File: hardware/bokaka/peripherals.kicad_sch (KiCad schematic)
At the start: 7 parts, among them SW1 SW_MEC_5G, SW2 SW_MEC_5G, SW3 SW_MEC_5G, U3 IS31FL3236A-TQ

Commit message: Finalize design before pcb
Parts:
- removed SW1, SW2, SW3: SW_MEC_5G, symbol Switch:SW_MEC_5G
- removed U3: IS31FL3236A-TQ, Package_QFP:TQFP-48-1EP_7x7mm_P0.5mm_EP4.11x4.11mm, symbol Driver_LED:IS31FL3236A-TQ
- added C12, C14, C22: 0.1u, Capacitor_SMD:C_0402_1005Metric, symbol Device:C
- added C13: 1u, Capacitor_SMD:C_0402_1005Metric, symbol Device:C
- added D10, D11, D12, D13, D14, D15, D16, D17, D18, D19, D2, D20, D21, D22, D23, D24, D25, D26, D27, D28, D29, D3, D30, D31, D32, D33, D34, D35, D36, D37, D38, D4, D5, D6, D7, D8, D9: LED, symbol Device:LED
- added R6: 1k5, Resistor_SMD:R_0402_1005Metric, symbol Device:R
- added R7: 10K, Resistor_SMD:R_0402_1005Metric, symbol Device:R
- added SW1, SW2, SW3: ~, EasyEDA_Lib:SW-SMD_4P-L5.1-W5.1-P3.70-LS6.5-TL_H1.5, symbol EasyEDA_Lib:TS-1187A-B-A-B
- added U1: IS31FL3236A-QFLS2-TR, Footprints:QFN40P500X500X80-45N, symbol Symbols:IS31FL3236A-QFLS2-TR
- BZ1: footprint (none) -> Footprints:CUI_CPT-9019S-SMT
- R4: footprint (none) -> Resistor_SMD:R_0402_1005Metric
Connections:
- net GND: now also C12.2, C13.2, C14.2, C22.2, R6.2, R7.2, SW1.4 (D), SW2.4 (D), SW3.4 (D), U1.17 (GND), U1.37 (AD), U1.39 (GND), U1.45 (EXP_PAD)
- net LED_I2C_SCL: now also U1.42 (SCL)
- net LED_I2C_SDA: now also U1.41 (SDA)
- net USR_BTN0: now also C14.1, SW2.1 (A)
- net USR_BTN1: now also C22.1, SW3.1 (A)
- net ~{BOOT_SEL}: now also SW1.1 (A)
- new net: D5.1 (K), U1.1 (OUT3)
- new net: D27.1 (K), U1.28 (OUT29)
- new net: D17.1 (K), U1.13 (OUT15)
- new net: R7.1, U1.40 (R_EXT)
- new net: D18.1 (K), U1.14 (OUT16)
- new net: D25.1 (K), U1.26 (OUT27)
- new net: D14.1 (K), U1.10 (OUT12)
- new net: D15.1 (K), U1.11 (OUT13)
- new net: D13.1 (K), U1.9 (OUT11)
- new net: D2.1 (K), R6.1
- new net: D20.1 (K), U1.16 (OUT18)
- new net: D11.1 (K), U1.7 (OUT9)
- new net: D26.1 (K), U1.27 (OUT28)
- new net: D6.1 (K), U1.2 (OUT4)
- new net: D16.1 (K), U1.12 (OUT14)
- new net: D19.1 (K), U1.15 (OUT17)
- new net: D38.1 (K), U1.35 (OUT36)
- new net: D7.1 (K), U1.3 (OUT5)
- new net: D33.1 (K), U1.22 (OUT23)
- new net: D28.1 (K), U1.29 (OUT30)
- new net: D22.1 (K), U1.19 (OUT20)
- new net: D21.1 (K), U1.18 (OUT19)
- new net: D32.1 (K), U1.31 (OUT32)
- new net: D23.1 (K), U1.24 (OUT25)
- new net: D9.1 (K), U1.5 (OUT7)
- new net: D12.1 (K), U1.8 (OUT10)
- new net: D29.1 (K), U1.20 (OUT21)
- new net: D31.1 (K), U1.21 (OUT22)
- new net: D36.1 (K), U1.23 (OUT24)
- new net: D24.1 (K), U1.25 (OUT26)
- new net: D30.1 (K), U1.30 (OUT31)
- new net: D34.1 (K), U1.32 (OUT33)
- new net: D37.1 (K), U1.33 (OUT34)
- new net: D35.1 (K), U1.34 (OUT35)
- new net: D8.1 (K), U1.4 (OUT6)
- new net: D4.1 (K), U1.44 (OUT2)
- new net: D10.1 (K), U1.6 (OUT8)
- new net +3V3: C12.1, C13.1, D10.2 (A), D11.2 (A), D12.2 (A), D13.2 (A), D14.2 (A), D15.2 (A), D16.2 (A), D17.2 (A), D18.2 (A), D19.2 (A), D20.2 (A), D21.2 (A), D22.2 (A), D23.2 (A), D24.2 (A), D25.2 (A), D26.2 (A), D27.2 (A), D28.2 (A), D29.2 (A), D3.2 (A), D30.2 (A), D31.2 (A), D32.2 (A), D33.2 (A), D34.2 (A), D35.2 (A), D36.2 (A), D37.2 (A), D38.2 (A), D4.2 (A), D5.2 (A), D6.2 (A), D7.2 (A), D8.2 (A), D9.2 (A), U1.38 (VCC)
- new net LED_DEBUG: D2.2 (A)
- new net LED_EN: U1.36 (SDB)
- new net PROGRESS_LED_0: D3.1 (K), U1.43 (OUT1)
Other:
- moved on the sheet: BZ1, D1, R4

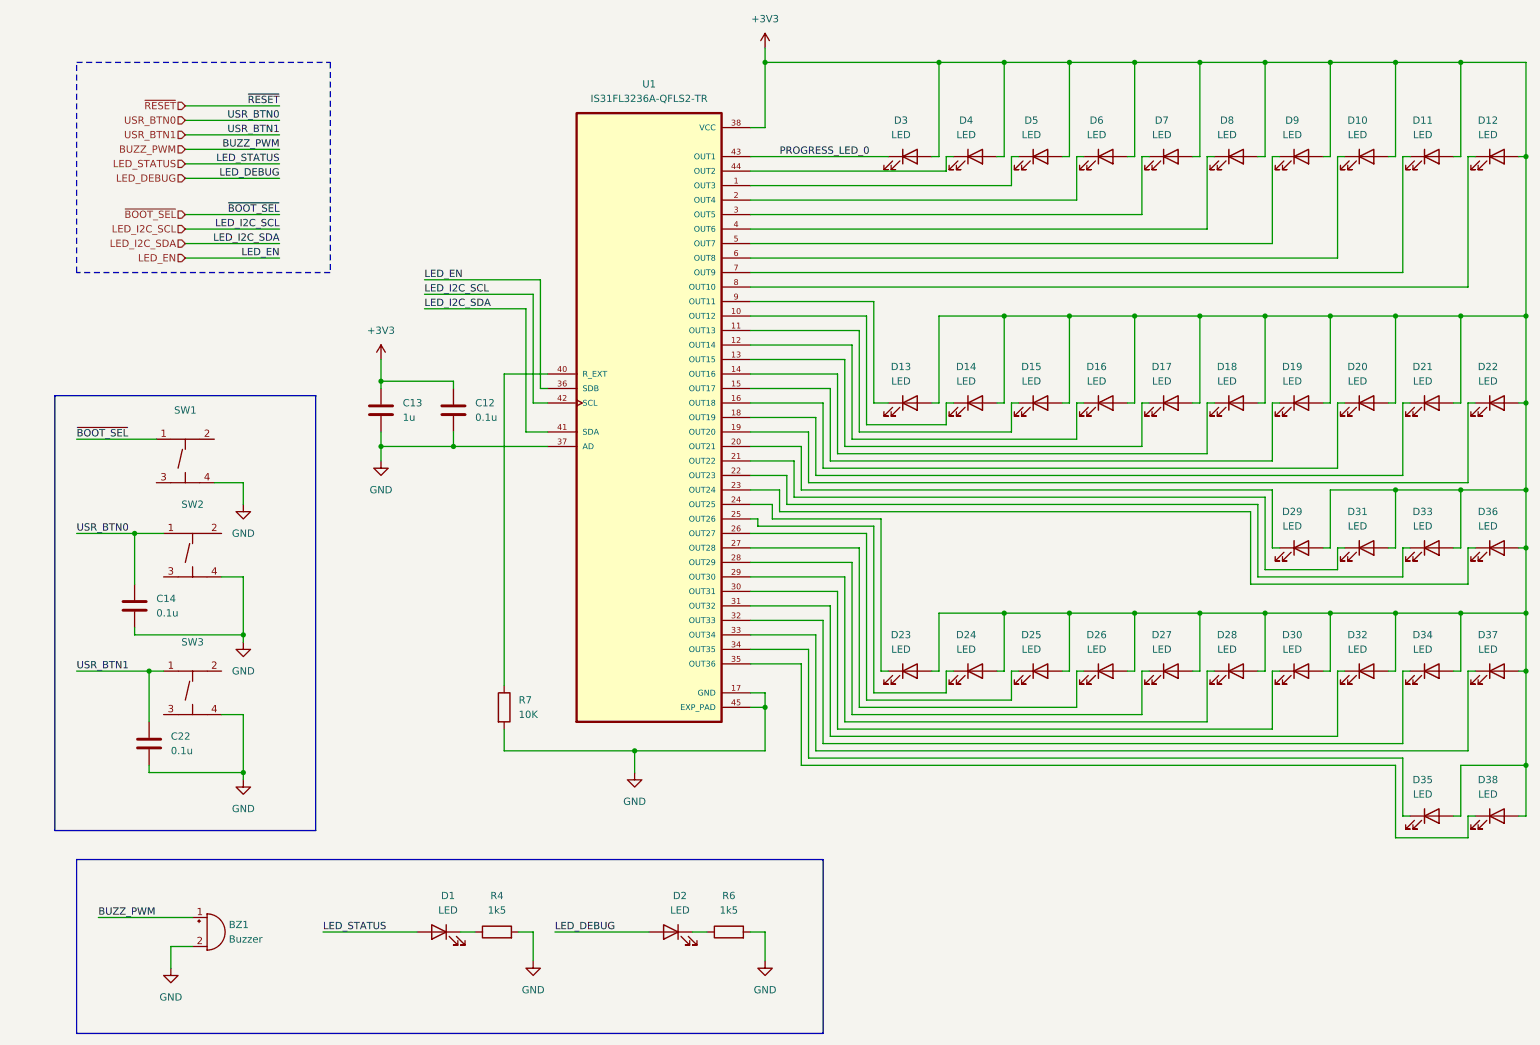
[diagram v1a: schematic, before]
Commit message: footprint asignment
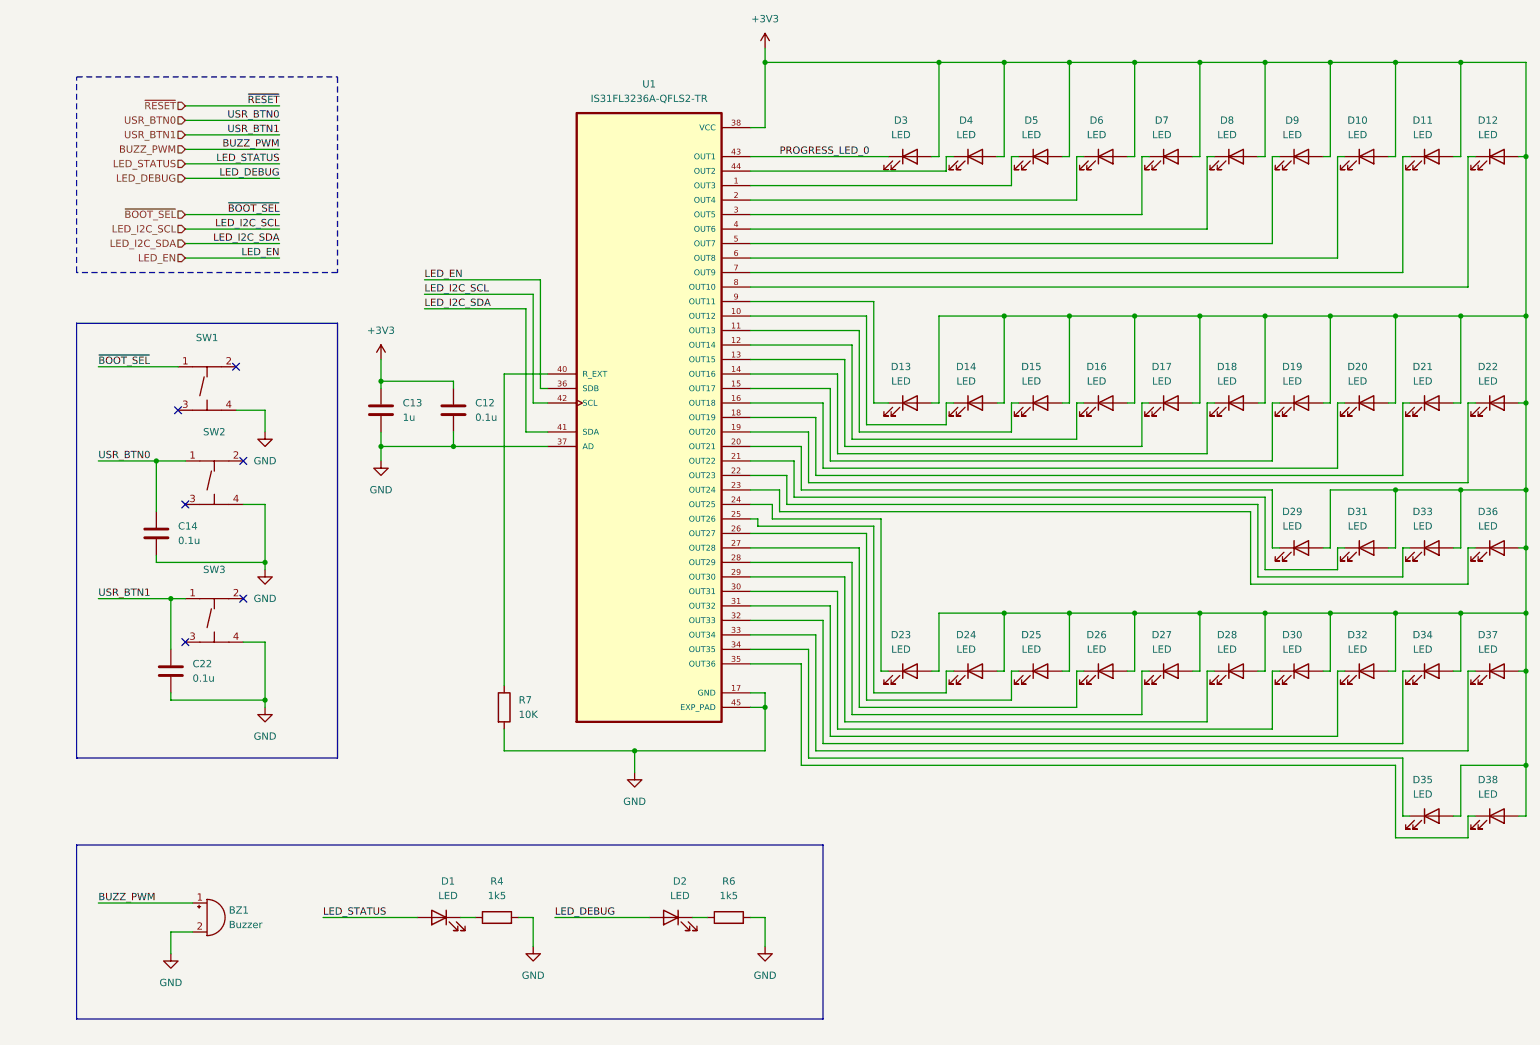
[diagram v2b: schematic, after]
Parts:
- removed SW1, SW2, SW3: ~, EasyEDA_Lib:SW-SMD_4P-L5.1-W5.1-P3.70-LS6.5-TL_H1.5, symbol EasyEDA_Lib:TS-1187A-B-A-B
- added SW1, SW2, SW3: ~, EasyEDA_Lib:SW-SMD_4P-L5.1-W5.1-P3.70-LS6.5-TL_H1.5, symbol Symbols:TS-1187A-B-A-B
- D1, D10, D11, D12, D13, D14, D15, D16, D17, D18, D19, D2, D20, D21, D22, D23, D24, D25, D26, D27, D28, D29, D3, D30, D31, D32, D33, D34, D35, D36, D37, D38, D4, D5, D6, D7, D8, D9: footprint (none) -> LED_SMD:LED_0603_1608Metric
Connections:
- net GND: now also SW1.4 (D), SW2.4 (D), SW3.4 (D)
- net USR_BTN0: now also SW2.1 (A)
- net USR_BTN1: now also SW3.1 (A)
- net ~{BOOT_SEL}: now also SW1.1 (A)
- no-connect marks 0 -> 6
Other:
- moved on the sheet: BZ1, C14, C22, D1, D2, R4, R6

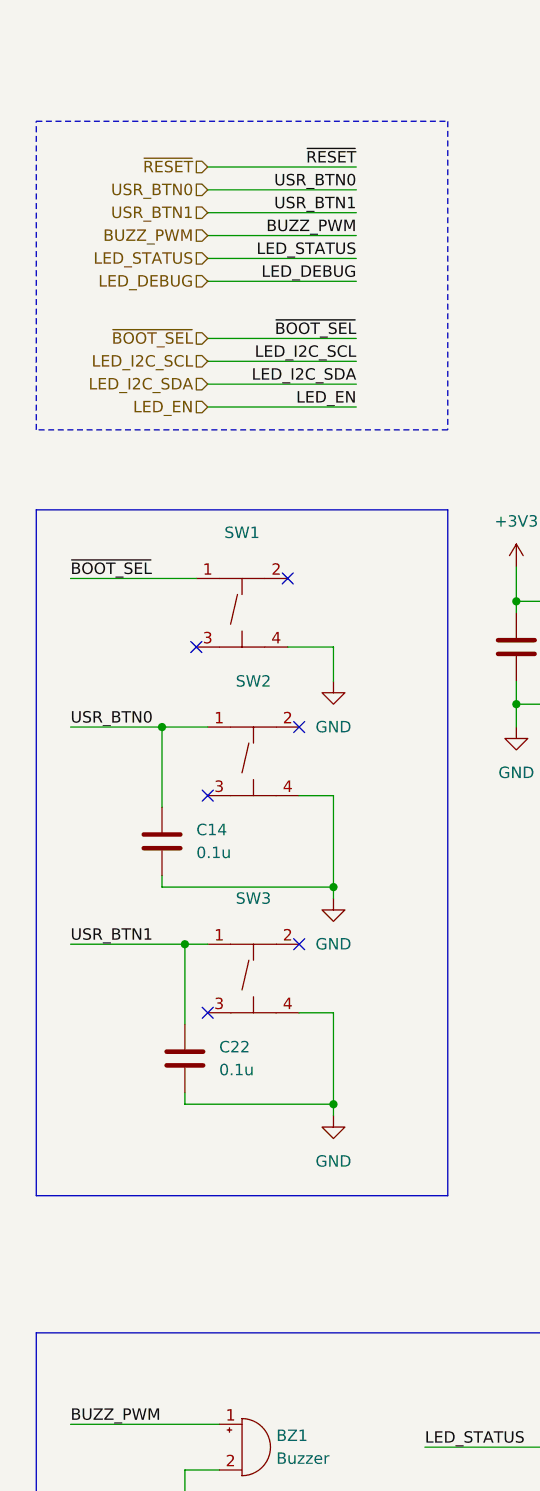
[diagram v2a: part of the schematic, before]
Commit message: schematic update
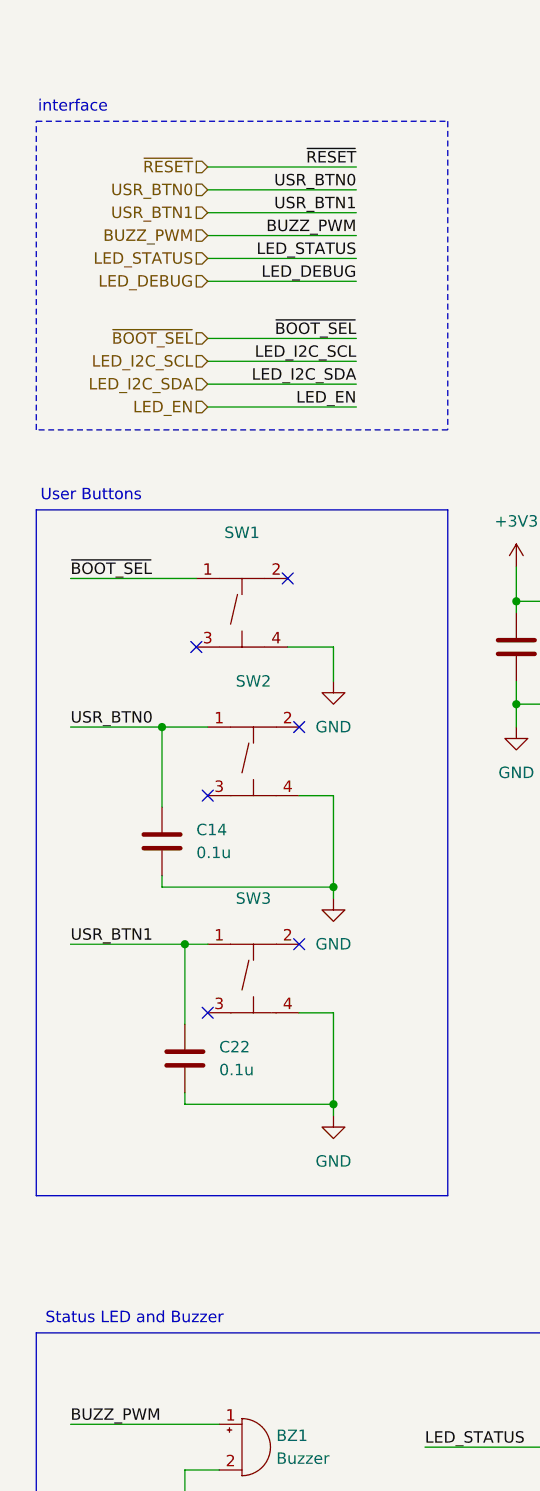
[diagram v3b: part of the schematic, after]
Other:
- note added: "Status LED and Buzzer"
- note added: "User Buttons"
- note added: "interface"
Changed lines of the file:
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@@
+		)
+	)
+	(text "Status LED and Buzzer"
+		(exclude_from_sim no)
+		(at 36.322 161.036 0)
+		(effects
+			(font
+				(size 1.27 1.27)
+			)
+		)
+	)
+	(text "User Buttons"
+		(exclude_from_sim no)
+		(at 31.496 69.596 0)
+		(effects
+			(font
+				(size 1.27 1.27)
+			)
+		)
+	)
+	(text "interface"
+		(exclude_from_sim no)
+		(at 29.464 26.416 0)
+		(effects
+			(font
+				(size 1.27 1.27)
+			)
 		)
 	)

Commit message: hardware update
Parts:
- added C2: 100n, Capacitor_SMD:C_0402_1005Metric, symbol Device:C
- added R2, R3: 10K, Resistor_SMD:R_0402_1005Metric, symbol Device:R
- added SW4: ~, EasyEDA_Lib:SW-SMD_4P-L5.1-W5.1-P3.70-LS6.5-TL_H1.5, symbol Symbols:TS-1187A-B-A-B
- C12, C14, C22: value 0.1u -> 100n
- C13: footprint Capacitor_SMD:C_0402_1005Metric -> Capacitor_SMD:C_0603_1608Metric
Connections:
- net +3V3: now also SW1.1 (A), SW1.2 (B), R2.1
- net GND: now also SW2.3 (C), SW3.3 (C), C2.2, R3.2, SW4.3 (C), SW4.4 (D); no longer SW1.4 (D)
- net USR_BTN0: now also SW3.1 (A), SW3.2 (B); no longer SW2.1 (A)
- net USR_BTN1: now also SW4.1 (A), SW4.2 (B); no longer SW3.1 (A)
- net ~{BOOT_SEL}: now also SW1.3 (C), SW1.4 (D), R3.1; no longer SW1.1 (A)
- net ~{RESET}: now also SW2.1 (A), SW2.2 (B), C2.1, R2.2
- no-connect marks 6 -> 0
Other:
- moved on the sheet: C12, C13, R7, SW1

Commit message: Devkit Production Ready
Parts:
- removed BZ1: Buzzer, Footprints:CUI_CPT-9019S-SMT, symbol Device:Buzzer
- added BUZZER1: ~, EasyEDA_Lib:BUZ-SMD_4P-L8.5-W8.5-P8.50-BR, symbol EasyEDA_Lib:MLT-8530
- added D39: LED, LED_SMD:LED_0603_1608Metric, symbol Device:LED
- added D40: BAT60A, Diode_SMD:D_SOD-323, symbol Diode:BAT60A
- added Q1: SS8050, Package_TO_SOT_SMD:SOT-23, symbol Transistor_BJT:SS8050
- added R16: 1k5, Resistor_SMD:R_0402_1005Metric, symbol Device:R
- added R17: 100, Resistor_SMD:R_0402_1005Metric, symbol Device:R
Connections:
- net +3V3: now also BUZZER1.1 (+), D39.2 (A), D40.1 (K)
- net BUZZ_PWM: now also R17.1
- net GND: now also Q1.2 (E), R16.2
- net PROGRESS_LED_2: now reaches D5.1 (K), U1.1 (OUT3)
- net ARM_LED_4: now reaches D27.1 (K), U1.28 (OUT29)
- net DISC_LED_4: now reaches D17.1 (K), U1.13 (OUT15)
- net DISC_LED_5: now reaches D18.1 (K), U1.14 (OUT16)
- net ARM_LED_2: now reaches D25.1 (K), U1.26 (OUT27)
- net DISC_LED_1: now reaches D14.1 (K), U1.10 (OUT12)
- net DISC_LED_2: now reaches D15.1 (K), U1.11 (OUT13)
- net DISC_LED_0: now reaches D13.1 (K), U1.9 (OUT11)
- net DISC_LED_7: now reaches D20.1 (K), U1.16 (OUT18)
- net PROGRESS_LED_8: now reaches D11.1 (K), U1.7 (OUT9)
- net ARM_LED_3: now reaches D26.1 (K), U1.27 (OUT28)
- net PROGRESS_LED_3: now reaches D6.1 (K), U1.2 (OUT4)
- net DISC_LED_3: now reaches D16.1 (K), U1.12 (OUT14)
- net DISC_LED_6: now reaches D19.1 (K), U1.15 (OUT17)
- net ARM_LED_11: now reaches D38.1 (K), U1.35 (OUT36)
- net PROGRESS_LED_4: now reaches D7.1 (K), U1.3 (OUT5)
- net DISC_LED_12: now reaches D33.1 (K), U1.22 (OUT23)
- net ARM_LED_5: now reaches D28.1 (K), U1.29 (OUT30)
- net DISC_LED_9: now reaches D22.1 (K), U1.19 (OUT20)
- net DISC_LED_8: now reaches D21.1 (K), U1.18 (OUT19)
- net ARM_LED_7: now reaches D32.1 (K), U1.31 (OUT32)
- net ARM_LED_0: now reaches D23.1 (K), U1.24 (OUT25)
- net PROGRESS_LED_6: now reaches D9.1 (K), U1.5 (OUT7)
- net PROGRESS_LED_9: now reaches D12.1 (K), U1.8 (OUT10)
- net DISC_LED_10: now reaches D29.1 (K), U1.20 (OUT21)
- net DISC_LED_11: now reaches D31.1 (K), U1.21 (OUT22)
- net DISC_LED_13: now reaches D36.1 (K), U1.23 (OUT24)
- net ARM_LED_1: now reaches D24.1 (K), U1.25 (OUT26)
- net ARM_LED_6: now reaches D30.1 (K), U1.30 (OUT31)
- net ARM_LED_8: now reaches D34.1 (K), U1.32 (OUT33)
- net ARM_LED_9: now reaches D37.1 (K), U1.33 (OUT34)
- net ARM_LED_10: now reaches D35.1 (K), U1.34 (OUT35)
- net PROGRESS_LED_5: now reaches D8.1 (K), U1.4 (OUT6)
- net PROGRESS_LED_1: now reaches D4.1 (K), U1.44 (OUT2)
- net PROGRESS_LED_7: now reaches D10.1 (K), U1.6 (OUT8)
- new net: Q1.1 (B), R17.2
- new net: BUZZER1.2, D40.2 (A), Q1.3 (C)
- new net LED_POWER: D39.1 (K), R16.1
- no-connect marks 0 -> 2
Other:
- moved on the sheet: C12, C13, C14, C2, C22, D1, D2, D23, D24, D25, D26, D27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
